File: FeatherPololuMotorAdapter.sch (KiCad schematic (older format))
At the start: 10 parts

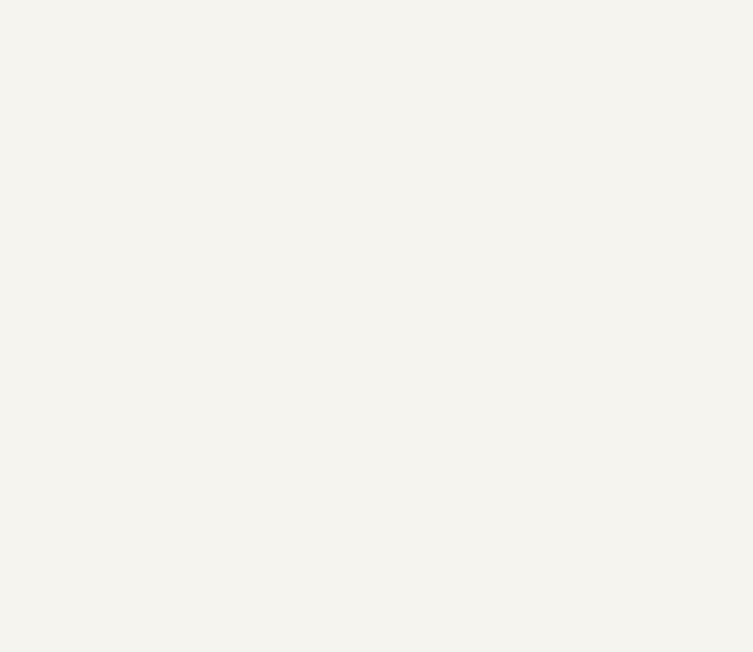
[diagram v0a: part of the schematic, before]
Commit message: Added generic feather component.
Stil working on schematic.
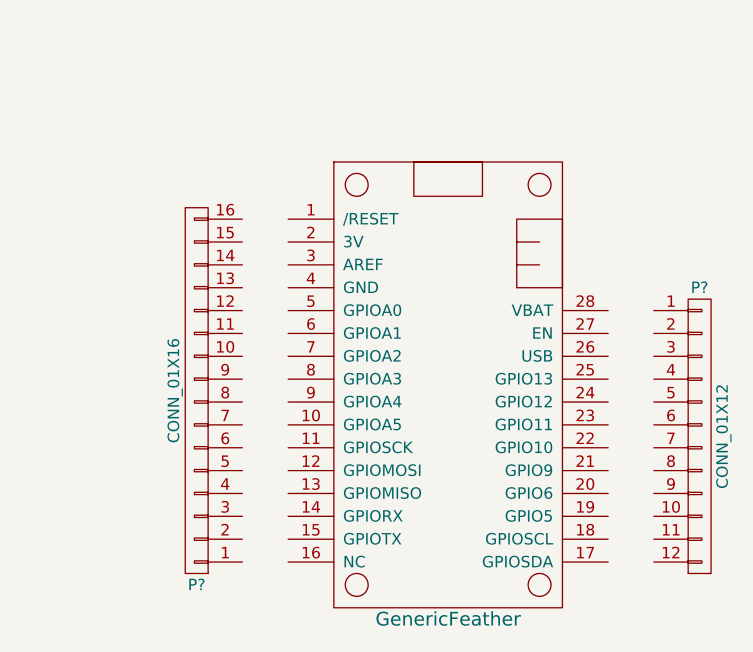
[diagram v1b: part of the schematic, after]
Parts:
- added P?: CONN_01X16, symbol CONN_01X16
- added P?: CONN_01X12, symbol CONN_01X12
- added U?: GenericFeather, symbol GenericFeather
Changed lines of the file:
@@
 LIBS:contrib
 LIBS:valves
+LIBS:schminktronics
+LIBS:FeatherPololuMotorAdapter-cache
 EELAYER 25 0
 EELAYER END
@@
 	1    0    0    -1
 $EndComp
+$Comp
+L GenericFeather U?
+U 1 1 59194204
+P 3650 5000
+F 0 "U?" H 3650 4150 60  0001 C CNN
+F 1 "GenericFeather" H 3650 4050 60  0000 C CNN
+F 2 "" H 3650 5000 60  0001 C CNN
+F 3 "" H 3650 5000 60  0001 C CNN
+	1    3650 5000
+	1    0    0    -1
+$EndComp
+$Comp
+L CONN_01X16 P?
+U 1 1 591943A4
+P 2550 4950
+F 0 "P?" H 2550 5800 50  0000 C CNN
+F 1 "CONN_01X16" V 2650 4950 50  0000 C CNN
+F 2 "" H 2550 4950 50  0000 C CNN
+F 3 "" H 2550 4950 50  0000 C CNN
+	1    2550 4950
+	-1   0    0    1
+$EndComp
+$Comp
+L CONN_01X12 P?
+U 1 1 591943FF
+P 4750 5150
+F 0 "P?" H 4750 5800 50  0000 C CNN
+F 1 "CONN_01X12" V 4850 5150 50  0000 C CNN
+F 2 "" H 4750 5150 50  0000 C CNN
+F 3 "" H 4750 5150 50  0000 C CNN
+	1    4750 5150
+	1    0    0    -1
+$EndComp

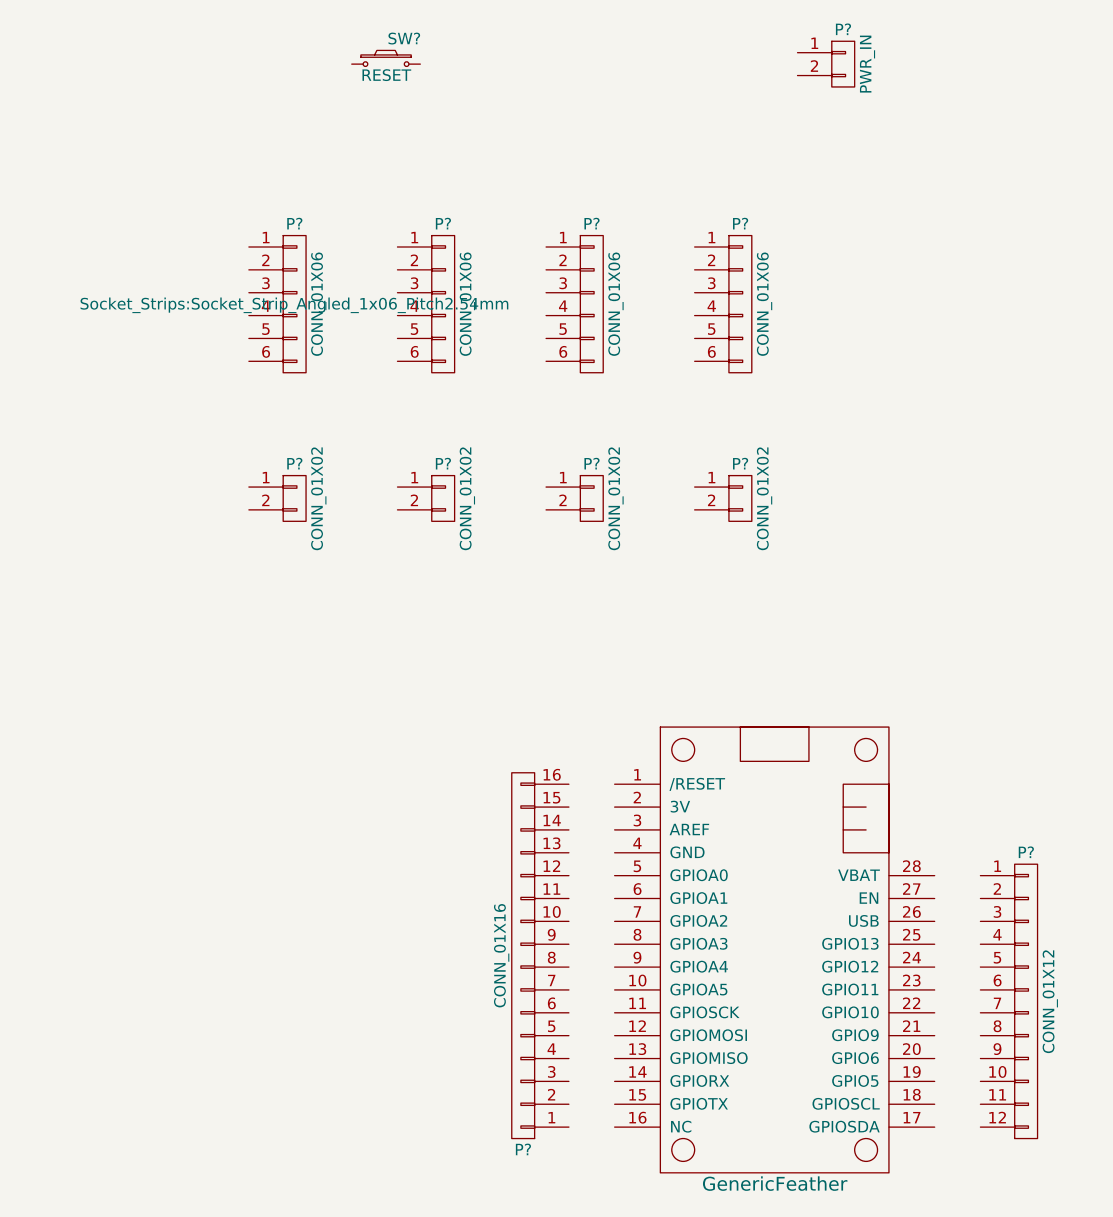
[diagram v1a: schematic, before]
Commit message: Finished schematic. Started work on layout.
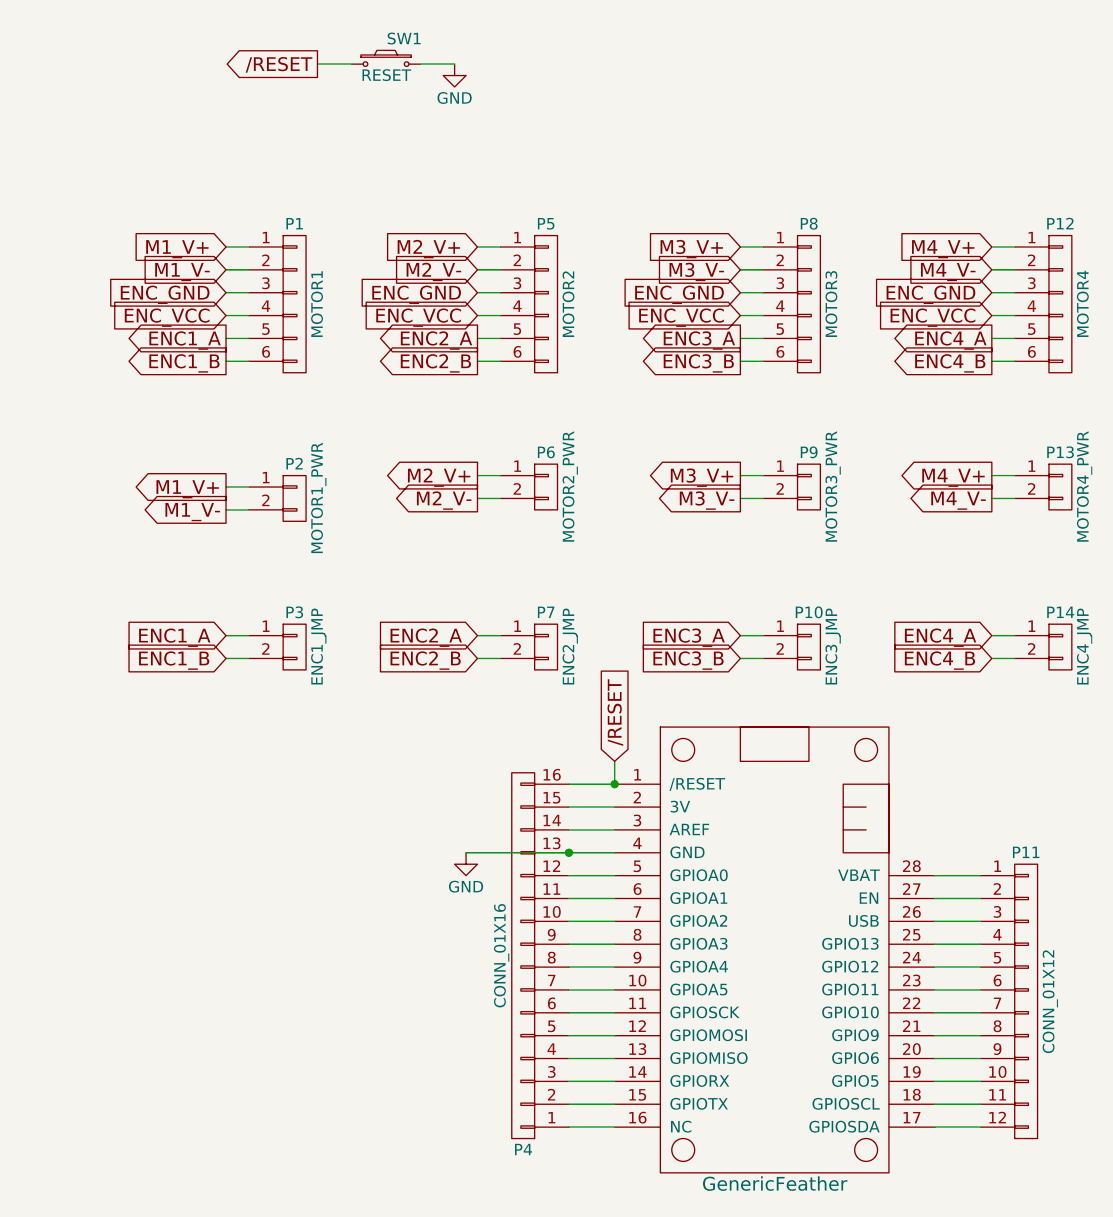
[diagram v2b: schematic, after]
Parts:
- removed P?: PWR_IN, symbol CONN_01X02
- added P10: ENC3_JMP, Pin_Headers:Pin_Header_Straight_1x02_Pitch2.54mm, symbol CONN_01X02
- added P14: ENC4_JMP, Pin_Headers:Pin_Header_Straight_1x02_Pitch2.54mm, symbol CONN_01X02
- added P3: ENC1_JMP, Pin_Headers:Pin_Header_Straight_1x02_Pitch2.54mm, symbol CONN_01X02
- added P7: ENC2_JMP, Pin_Headers:Pin_Header_Straight_1x02_Pitch2.54mm, symbol CONN_01X02
- P1: renamed from P?; value CONN_01X06 -> MOTOR1; footprint Socket_Strips:Socket_Strip_Angled_1x06_Pitch2.54mm -> Pin_Headers:Pin_Header_Angled_1x06_Pitch2.54mm
- P11: renamed from P?; footprint (none) -> Pin_Headers:Pin_Header_Straight_1x12_Pitch2.54mm
- P12: renamed from P?; value CONN_01X06 -> MOTOR4; footprint (none) -> Pin_Headers:Pin_Header_Angled_1x06_Pitch2.54mm
- P13: renamed from P?; value CONN_01X02 -> MOTOR4_PWR; footprint (none) -> Terminal_Blocks:TerminalBlock_Pheonix_PT-3.5mm_2pol
- P2: renamed from P?; value CONN_01X02 -> MOTOR1_PWR; footprint (none) -> Terminal_Blocks:TerminalBlock_Pheonix_PT-3.5mm_2pol
- P4: renamed from P?; footprint (none) -> Pin_Headers:Pin_Header_Straight_1x16_Pitch2.54mm
- P5: renamed from P?; value CONN_01X06 -> MOTOR2; footprint (none) -> Pin_Headers:Pin_Header_Angled_1x06_Pitch2.54mm
- P6: renamed from P?; value CONN_01X02 -> MOTOR2_PWR; footprint (none) -> Terminal_Blocks:TerminalBlock_Pheonix_PT-3.5mm_2pol
- P8: renamed from P?; value CONN_01X06 -> MOTOR3; footprint (none) -> Pin_Headers:Pin_Header_Angled_1x06_Pitch2.54mm
- P9: renamed from P?; value CONN_01X02 -> MOTOR3_PWR; footprint (none) -> Terminal_Blocks:TerminalBlock_Pheonix_PT-3.5mm_2pol
- SW1: renamed from SW?; footprint (none) -> Buttons_Switches_ThroughHole:SW_PUSH_6mm
- U1: renamed from U?; footprint (none) -> schminktronics:Adafruit_Feather
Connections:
- net M1_V+: now reaches P1.1 (P1)
- net M1_V+: now also P2.1 (P1)
- net M1_V-: now reaches P1.2 (P2)
- net M1_V-: now also P2.2 (P2)
- net ENC_GND: now reaches P1.3 (P3)
- net ENC_GND: now also P12.3 (P3), P5.3 (P3), P8.3 (P3)
- net ENC_VCC: now reaches P1.4 (P4)
- net ENC_VCC: now also P12.4 (P4), P5.4 (P4), P8.4 (P4)
- net ENC1_A: now reaches P1.5 (P5)
- net ENC1_A: now also P3.1 (P1)
- net ENC1_B: now reaches P1.6 (P6)
- net ENC1_B: now also P3.2 (P2)
- net M2_V+: now reaches P5.1 (P1)
- net M2_V+: now also P6.1 (P1)
- net M2_V-: now reaches P5.2 (P2)
- net M2_V-: now also P6.2 (P2)
- net ENC2_A: now reaches P5.5 (P5)
- net ENC2_A: now also P7.1 (P1)
- net ENC2_B: now reaches P5.6 (P6)
- net ENC2_B: now also P7.2 (P2)
- net M3_V+: now reaches P8.1 (P1)
- net M3_V+: now also P9.1 (P1)
- net M3_V-: now reaches P8.2 (P2)
- net M3_V-: now also P9.2 (P2)
- net ENC3_A: now reaches P8.5 (P5)
- net ENC3_A: now also P10.1 (P1)
- net ENC3_B: now reaches P8.6 (P6)
- net ENC3_B: now also P10.2 (P2)
- net M4_V+: now reaches P12.1 (P1)
- net M4_V+: now also P13.1 (P1)
- net M4_V-: now reaches P12.2 (P2)
- net M4_V-: now also P13.2 (P2)
- net ENC4_A: now reaches P12.5 (P5)
- net ENC4_A: now also P14.1 (P1)
- net ENC4_B: now reaches P12.6 (P6)
- net ENC4_B: now also P14.2 (P2)
- net /RESET: now reaches SW1.1
- net /RESET: now also P4.16 (P16), U1.1 (/RESET)
- net GND: now reaches SW1.2
- net GND: now also P4.13 (P13), U1.4 (GND)
- net at U1.10 (GPIOA5): now also P4.7 (P7)
- net at U1.11 (GPIOSCK): now also P4.6 (P6)
- net at U1.12 (GPIOMOSI): now also P4.5 (P5)
- net at U1.13 (GPIOMISO): now also P4.4 (P4)
- net at U1.14 (GPIORX): now also P4.3 (P3)
- net at U1.15 (GPIOTX): now also P4.2 (P2)
- net at U1.16 (NC): now also P4.1 (P1)
- net at U1.17 (GPIOSDA): now also P11.12 (P12)
- net at U1.18 (GPIOSCL): now also P11.11 (P11)
- net at U1.19 (GPIO5): now also P11.10 (P10)
- net at U1.2 (3V): now also P4.15 (P15)
- net at U1.20 (GPIO6): now also P11.9 (P9)
- net at U1.21 (GPIO9): now also P11.8 (P8)
- net at U1.22 (GPIO10): now also P11.7 (P7)
- net at U1.23 (GPIO11): now also P11.6 (P6)
- net at U1.24 (GPIO12): now also P11.5 (P5)
- net at U1.25 (GPIO13): now also P11.4 (P4)
- net at U1.26 (USB): now also P11.3 (P3)
- net at U1.27 (EN): now also P11.2 (P2)
- net at U1.28 (VBAT): now also P11.1 (P1)
- net at U1.3 (AREF): now also P4.14 (P14)
- net at U1.5 (GPIOA0): now also P4.12 (P12)
- net at U1.6 (GPIOA1): now also P4.11 (P11)
- net at U1.7 (GPIOA2): now also P4.10 (P10)
- net at U1.8 (GPIOA3): now also P4.9 (P9)
- net at U1.9 (GPIOA4): now also P4.8 (P8)
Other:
- moved on the sheet: P12, P13, P5, P6, P8, P9

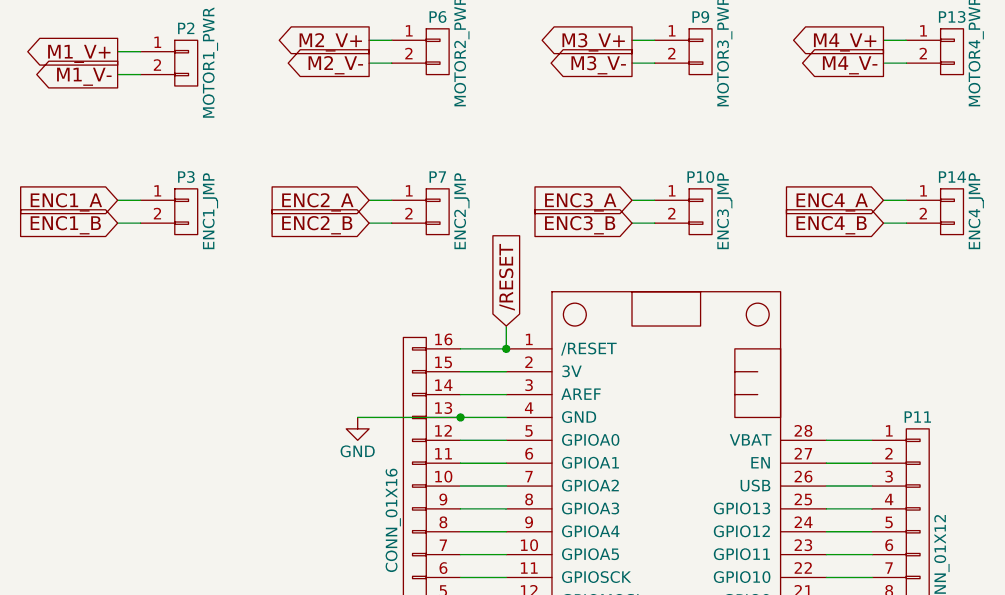
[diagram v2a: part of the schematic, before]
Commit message: Finished schematic and layout.
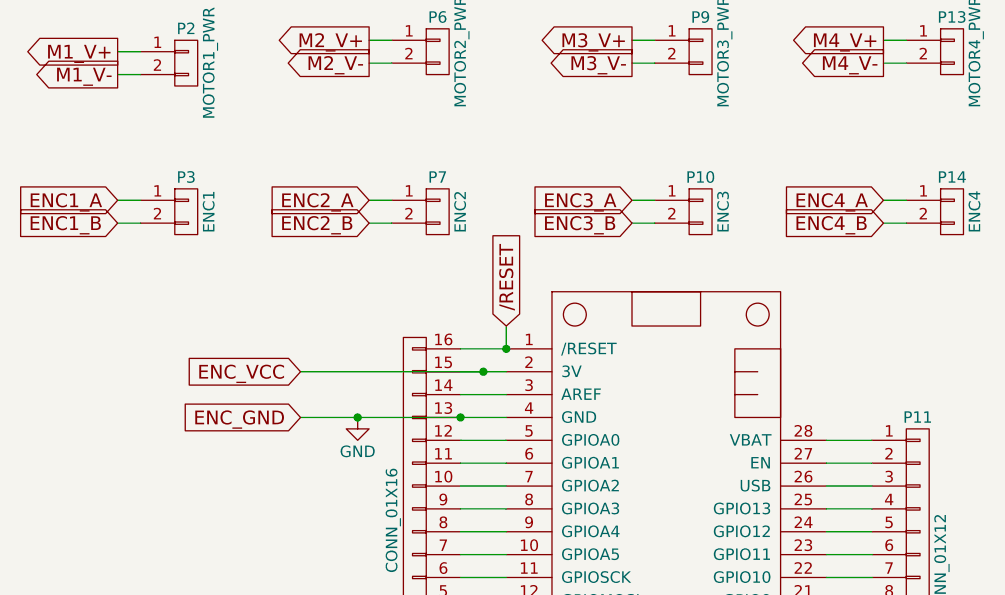
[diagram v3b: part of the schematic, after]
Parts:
- P1, P12, P5, P8: footprint Pin_Headers:Pin_Header_Angled_1x06_Pitch2.54mm -> Pin_Headers:Pin_Header_Straight_1x06_Pitch2.54mm
- P10: value ENC3_JMP -> ENC3
- P14: value ENC4_JMP -> ENC4
- P3: value ENC1_JMP -> ENC1
- P7: value ENC2_JMP -> ENC2
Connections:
- net ENC_GND is gone; now on net GND: P1.3 (P3), P12.3 (P3), P5.3 (P3), P8.3 (P3)
- net ENC_VCC: now also P4.15 (P15), U1.2 (3V)
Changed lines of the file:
@@
 F 0 "P1" H 1550 2450 50  0000 C CNN
 F 1 "MOTOR1" V 1650 2100 50  0000 C CNN
-F 2 "Pin_Headers:Pin_Header_Angled_1x06_Pitch2.54mm" V 1200 2000 50  0001 C CNN
+F 2 "Pin_Headers:Pin_Header_Straight_1x06_Pitch2.54mm" V 1200 2000 50  0001 C CNN
 F 3 "" H 1550 2100 50  0000 C CNN
 	1    1550 2100
@@
 F 0 "P5" H 2650 2450 50  0000 C CNN
 F 1 "MOTOR2" V 2750 2100 50  0000 C CNN
-F 2 "Pin_Headers:Pin_Header_Angled_1x06_Pitch2.54mm" V 2650 2100 50  0001 C CNN
+F 2 "Pin_Headers:Pin_Header_Straight_1x06_Pitch2.54mm" V 2650 2100 50  0001 C CNN
 F 3 "" H 2650 2100 50  0000 C CNN
 	1    2650 2100
@@
 F 0 "P8" H 3800 2450 50  0000 C CNN
 F 1 "MOTOR3" V 3900 2100 50  0000 C CNN
-F 2 "Pin_Headers:Pin_Header_Angled_1x06_Pitch2.54mm" V 3800 2100 50  0001 C CNN
+F 2 "Pin_Headers:Pin_Header_Straight_1x06_Pitch2.54mm" V 3800 2100 50  0001 C CNN
 F 3 "" H 3800 2100 50  0000 C CNN
 	1    3800 2100
@@
 F 0 "P12" H 4900 2450 50  0000 C CNN
 F 1 "MOTOR4" V 5000 2100 50  0000 C CNN
-F 2 "Pin_Headers:Pin_Header_Angled_1x06_Pitch2.54mm" V 4900 2100 50  0001 C CNN
+F 2 "Pin_Headers:Pin_Header_Straight_1x06_Pitch2.54mm" V 4900 2100 50  0001 C CNN
 F 3 "" H 4900 2100 50  0000 C CNN
 	1    4900 2100
@@
 	2750 4400 2950 4400
 Wire Wire Line
-	2300 4500 2950 4500
+	2050 4500 2950 4500
 Wire Wire Line
 	2750 4600 2950 4600
@@
 P 1550 3600
 F 0 "P3" H 1550 3750 50  0000 C CNN
-F 1 "ENC1_JMP" V 1650 3600 50  0000 C CNN
+F 1 "ENC1" V 1650 3600 50  0000 C CNN
 F 2 "Pin_Headers:Pin_Header_Straight_1x02_Pitch2.54mm" V 1750 3450 50  0001 C CNN
 F 3 "" H 1550 3600 50  0000 C CNN
@@
 P 2650 3600
 F 0 "P7" H 2650 3750 50  0000 C CNN
-F 1 "ENC2_JMP" V 2750 3600 50  0000 C CNN
+F 1 "ENC2" V 2750 3600 50  0000 C CNN
 F 2 "Pin_Headers:Pin_Header_Straight_1x02_Pitch2.54mm" V 2650 3600 50  0001 C CNN
 F 3 "" H 2650 3600 50  0000 C CNN
@@
 P 3800 3600
 F 0 "P10" H 3800 3750 50  0000 C CNN
-F 1 "ENC3_JMP" V 3900 3600 50  0000 C CNN
+F 1 "ENC3" V 3900 3600 50  0000 C CNN
 F 2 "Pin_Headers:Pin_Header_Straight_1x02_Pitch2.54mm" V 3800 3600 50  0001 C CNN
 F 3 "" H 3800 3600 50  0000 C CNN
@@
 P 4900 3600
 F 0 "P14" H 4900 3750 50  0000 C CNN
-F 1 "ENC4_JMP" V 5000 3600 50  0000 C CNN
+F 1 "ENC4" V 5000 3600 50  0000 C CNN
 F 2 "Pin_Headers:Pin_Header_Straight_1x02_Pitch2.54mm" V 4900 3600 50  0001 C CNN
 F 3 "" H 4900 3600 50  0000 C CNN
@@
 Connection ~ 2750 4500
 Connection ~ 2950 4200
+Text GLabel 2050 4500 0    60   Input ~ 0
+ENC_GND
+Text GLabel 2050 4300 0    60   Input ~ 0
+ENC_VCC
+Connection ~ 2300 4500
+Wire Wire Line
+	2050 4300 2850 4300
+Connection ~ 2850 4300
 $EndSCHEMATC
